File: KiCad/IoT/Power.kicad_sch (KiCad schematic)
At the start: 4 parts, among them J10 5V, J11 3V3, J8 24V, J9 12V

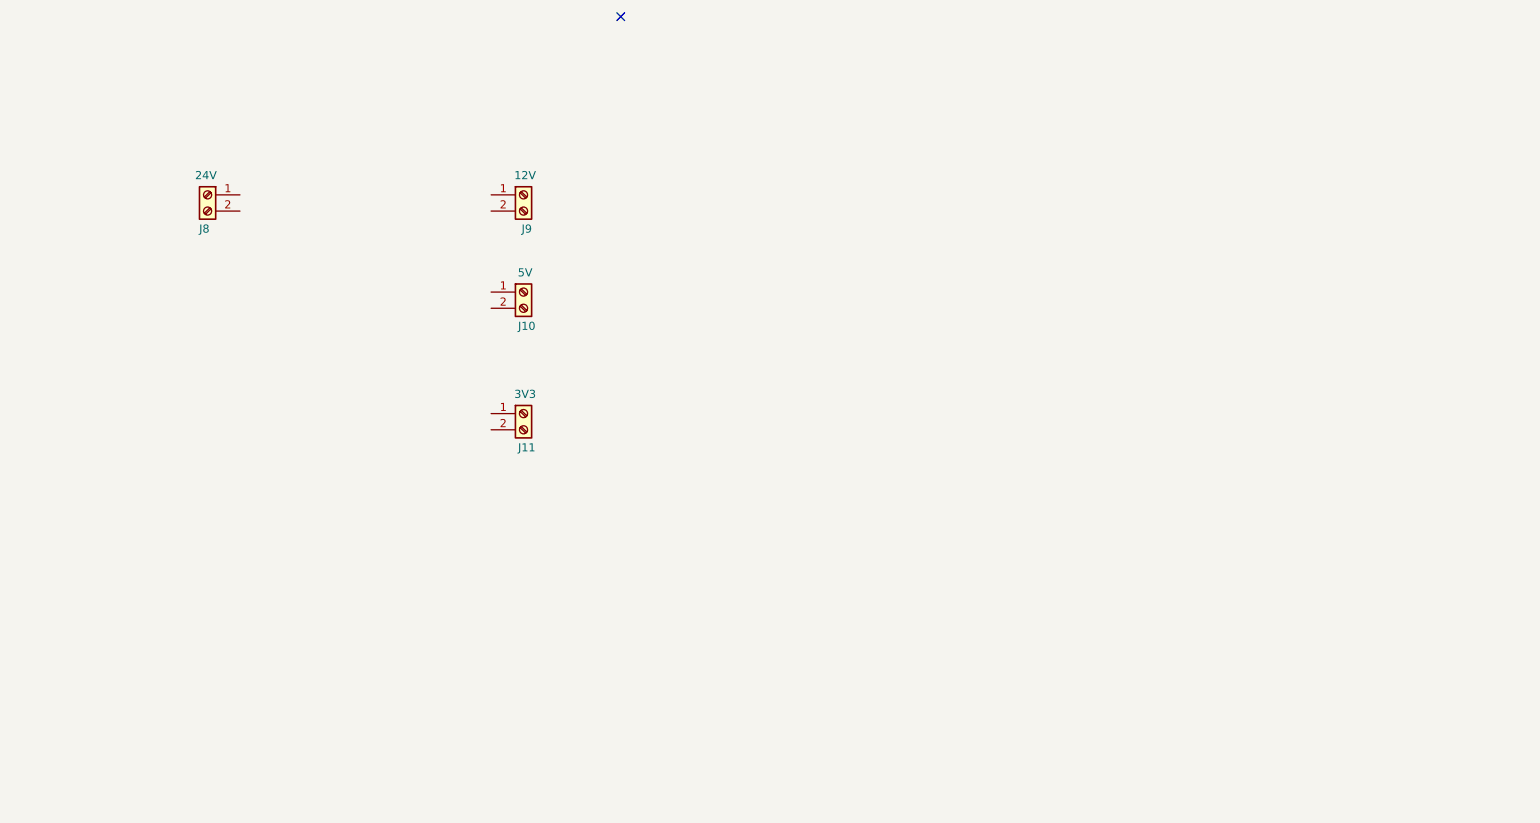
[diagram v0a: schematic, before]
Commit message: updated power schematic
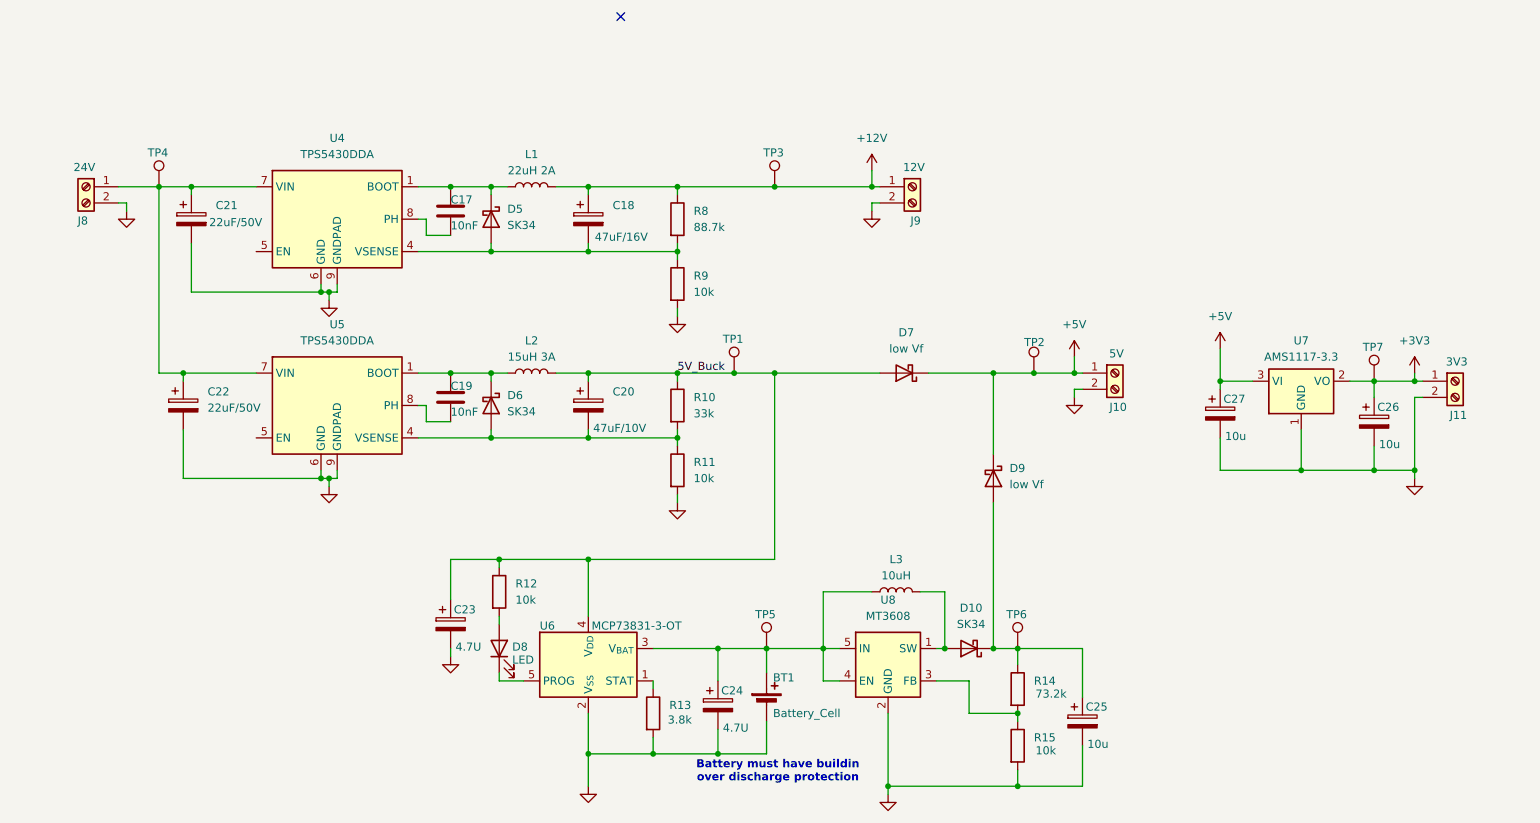
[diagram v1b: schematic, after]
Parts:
- added BT1: Battery_Cell, Battery:BatteryHolder_MPD_BH-18650-PC, symbol Device:Battery_Cell
- added C17, C19: 10nF, symbol Device:C
- added C18: 47uF/16V, Package_SO:SOIC-8_3.9x4.9mm_P1.27mm, symbol Device:C_Polarized
- added C20: 47uF/10V, Package_SO:SOIC-8_3.9x4.9mm_P1.27mm, symbol Device:C_Polarized
- added C21, C22: 22uF/50V, Package_SO:SOIC-8_3.9x4.9mm_P1.27mm, symbol Device:C_Polarized
- added C23, C24: 4.7U, Package_SO:SOIC-8_3.9x4.9mm_P1.27mm, symbol Device:C_Polarized
- added C25, C26, C27: 10u, Package_SO:SOIC-8_3.9x4.9mm_P1.27mm, symbol Device:C_Polarized
- added D10, D5, D6: SK34, Package_SON:WSON-8-1EP_6x5mm_P1.27mm_EP3.4x4mm, symbol Device:D_Schottky
- added D7, D9: low Vf, Package_SON:WSON-8-1EP_6x5mm_P1.27mm_EP3.4x4mm, symbol Device:D_Schottky
- added D8: LED, LED_SMD:LED_Cree-XHP50_3V_HighDensity, symbol Device:LED
- added L1: 22uH 2A, symbol Device:L
- added L2: 15uH 3A, symbol Device:L
- added L3: 10uH, Package_TO_SOT_SMD:SOT-23-6, symbol Device:L
- added R10: 33k, symbol Device:R
- added R11, R12, R15, R9: 10k, symbol Device:R
- added R13: 3.8k, symbol Device:R
- added R14: 73.2k, symbol Device:R
- added R8: 88.7k, symbol Device:R
- added TP1, TP2, TP3, TP4, TP5, TP6, TP7: TestPoint, Connector_Pin:Pin_D0.7mm_L6.5mm_W1.8mm_FlatFork, symbol Connector:TestPoint
- added U4, U5: TPS5430DDA, Package_SO:TI_SO-PowerPAD-8_ThermalVias, symbol Regulator_Switching:TPS5430DDA
- added U6: MCP73831-3-OT, Package_TO_SOT_SMD:SOT-23-5, symbol Battery_Management:MCP73831-3-OT
- added U7: AMS1117-3.3, Package_TO_SOT_SMD:SOT-223-3_TabPin2, symbol Regulator_Linear:AMS1117-3.3
- added U8: MT3608, Package_TO_SOT_SMD:SOT-23-6, symbol Regulator_Switching:MT3608
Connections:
- net +12V: now reaches J9.1 (Pin_1)
- net +12V: now also C18.1, L1.2, R8.1, TP3.1
- net GND: now reaches J9.2 (Pin_2)
- net GND: now also J10.2 (Pin_2), J11.2 (Pin_2), J8.2 (Pin_2), BT1.2 (-), C21.2, C22.2, C23.2, C24.2, C25.2, C26.2, C27.2, R11.2, R13.2, R15.2, R9.2, U4.6 (GND), U4.9 (GNDPAD), U5.6 (GND), U5.9 (GNDPAD), U6.2 (V_{SS}), U7.1 (GND), U8.2 (GND)
- net +5V: now reaches J10.1 (Pin_1)
- net +5V: now also C27.1, D7.1 (K), D9.1 (K), TP2.1, U7.3 (VI)
- net +3V3: now reaches J11.1 (Pin_1)
- net +3V3: now also C26.1, TP7.1, U7.2 (VO)
- net at J8.1 (Pin_1): now also C21.1, C22.1, TP4.1, U4.7 (VIN), U5.7 (VIN)
- new net: C18.2, D5.2 (A), R8.2, R9.1, U4.4 (VSENSE)
- new net: C25.1, D10.1 (K), D9.2 (A), R14.1, TP6.1
- new net: C19.1, D6.1 (K), L2.1, U5.1 (BOOT)
- new net: C20.2, D6.2 (A), R10.2, R11.1, U5.4 (VSENSE)
- new net: R14.2, R15.1, U8.3 (FB)
- new net: D10.2 (A), L3.2, U8.1 (SW)
- new net: BT1.1 (+), C24.1, L3.1, TP5.1, U6.3 (V_{BAT}), U8.4 (EN), U8.5 (IN)
- new net: C17.1, D5.1 (K), L1.1, U4.1 (BOOT)
- new net: D8.2 (A), R12.2
- new net: C19.2, U5.8 (PH)
- new net: R13.1, U6.1 (STAT)
- new net: D8.1 (K), U6.5 (PROG)
- new net: C17.2, U4.8 (PH)
- new net 5V_Buck: C20.1, C23.1, D7.2 (A), L2.2, R10.1, R12.1, TP1.1, U6.4 (V_{DD})
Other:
- note added: "Battery must have buildin over discharge protection"
- moved on the sheet: J10, J11, J8, J9

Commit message: added buttons, connected leds, changed uart ic and added crystals
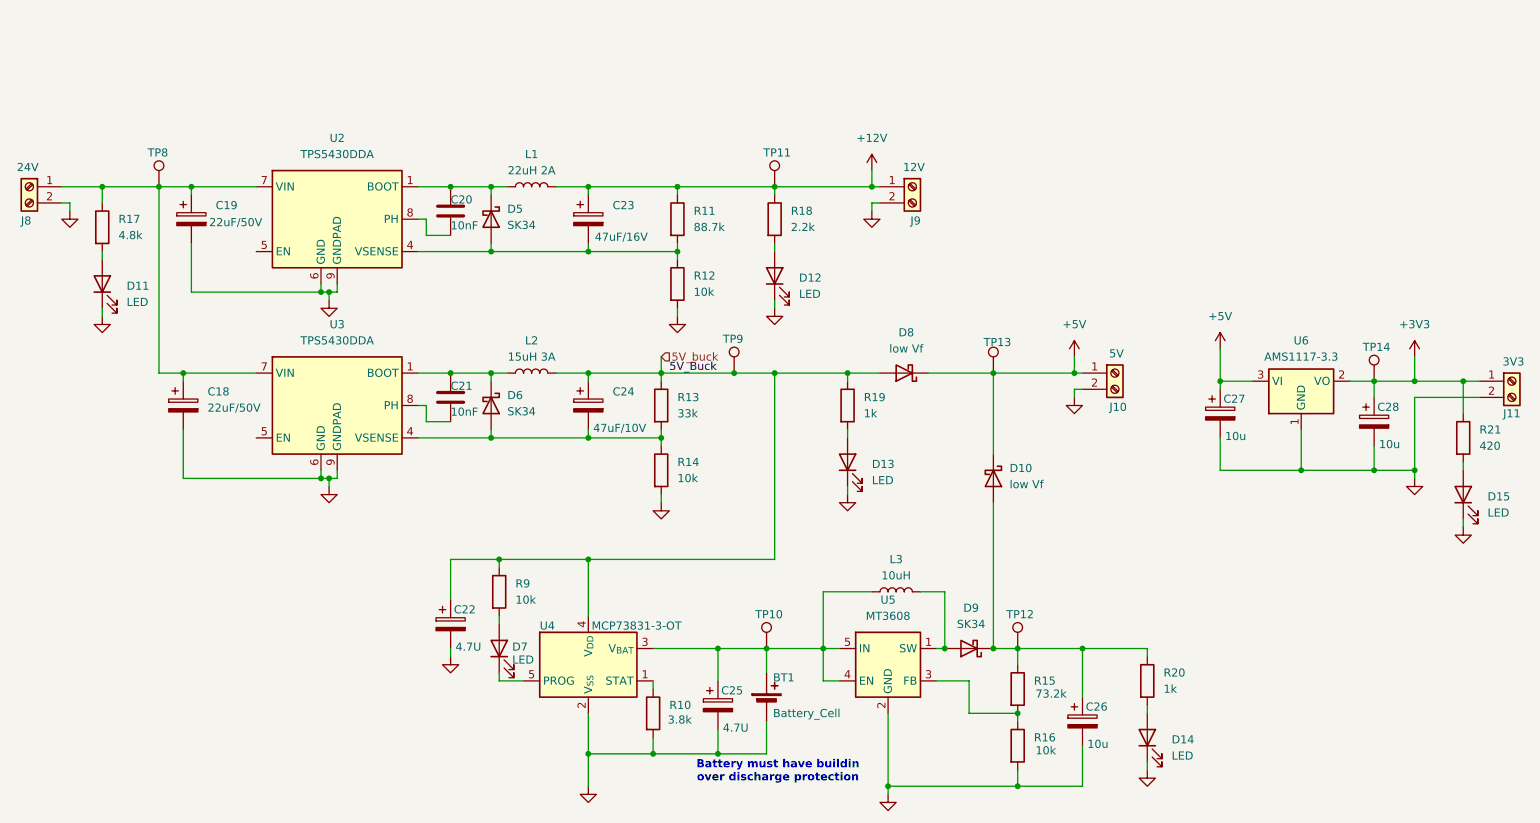
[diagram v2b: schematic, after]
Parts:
- added D11, D12, D13, D14, D15: LED, symbol Device:LED
- added R17: 4.8k, symbol Device:R
- added R18: 2.2k, symbol Device:R
- added R19, R20: 1k, symbol Device:R
- added R21: 420, symbol Device:R
- C19: renamed from C21; footprint Package_SO:SOIC-8_3.9x4.9mm_P1.27mm -> (none)
- C20: renamed from C17; footprint (none) -> Capacitor_SMD:C_0603_1608Metric
- C21: renamed from C19; footprint (none) -> Capacitor_SMD:C_0603_1608Metric
- C22: renamed from C23; footprint Package_SO:SOIC-8_3.9x4.9mm_P1.27mm -> (none)
- C23: renamed from C18; footprint Package_SO:SOIC-8_3.9x4.9mm_P1.27mm -> (none)
- C24: renamed from C20; footprint Package_SO:SOIC-8_3.9x4.9mm_P1.27mm -> (none)
- C25: renamed from C24; footprint Package_SO:SOIC-8_3.9x4.9mm_P1.27mm -> (none)
- C26: renamed from C25; footprint Package_SO:SOIC-8_3.9x4.9mm_P1.27mm -> (none)
- C27: footprint Package_SO:SOIC-8_3.9x4.9mm_P1.27mm -> (none)
- C28: renamed from C26; footprint Package_SO:SOIC-8_3.9x4.9mm_P1.27mm -> (none)
- D10: renamed from D9; footprint Package_SON:WSON-8-1EP_6x5mm_P1.27mm_EP3.4x4mm -> (none)
- D5, D6: footprint Package_SON:WSON-8-1EP_6x5mm_P1.27mm_EP3.4x4mm -> (none)
- D7: renamed from D8; footprint LED_SMD:LED_Cree-XHP50_3V_HighDensity -> (none)
- D8: renamed from D7; footprint Package_SON:WSON-8-1EP_6x5mm_P1.27mm_EP3.4x4mm -> (none)
- D9: renamed from D10; footprint Package_SON:WSON-8-1EP_6x5mm_P1.27mm_EP3.4x4mm -> (none)
- renumbered C22 to C18, R13 to R10, R8 to R11, R9 to R12, R10 to R13, R11 to R14, R14 to R15, R15 to R16, R12 to R9, TP5 to TP10, TP3 to TP11, TP6 to TP12, TP2 to TP13, TP7 to TP14, TP4 to TP8, TP1 to TP9, U4 to U2, U5 to U3, U6 to U4, U8 to U5, U7 to U6
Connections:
- net +12V: now also R18.1
- net +3V3: now also R21.1
- net GND: now also D11.1 (K), D12.1 (K), D13.1 (K), D14.1 (K), D15.1 (K)
- net at C26.1, D10.2 (A), D9.1 (K)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: now also R20.1
- net at C18.1, C19.1, J8.1 (Pin_1)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: now also R17.1
- net 5V_Buck renamed 5V_buck
- net 5V_buck: now also R19.1
- new net: D11.2 (A), R17.2
- new net: D12.2 (A), R18.2
- new net: D14.2 (A), R20.2
- new net: D15.2 (A), R21.2
- new net: D13.2 (A), R19.2
- no-connect marks 1 -> 0
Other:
- moved on the sheet: J11, J8, R13, R14, TP13

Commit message: minor fixes and cleanup
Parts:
- renumbered C18 to C23, C19 to C24, C20 to C25, C21 to C26, C22 to C27, C23 to C28, C24 to C29, C25 to C30, C26 to C31, C27 to C32, C28 to C33, D12 to D10, D13 to D11, D8 to D12, D9 to D13, D10 to D14, D14 to D15, D15 to D16, D11 to D6, D5 to D7, D6 to D8, D7 to D9, J9 to J10, J10 to J11, J11 to J12, J8 to J9, R17 to R16, R9 to R17, R10 to R18, R13 to R19, R14 to R20, R11 to R21, R12 to R22, R18 to R23, R19 to R24, R15 to R25, R16 to R26, R20 to R27, R21 to R28, TP13 to TP12, TP12 to TP13

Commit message: circuit bugfixes
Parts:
- C34: renamed from C33; value 10u -> 22u
- renumbered C23 to C24, C24 to C25, C25 to C26, C26 to C27, C27 to C28, C28 to C29, C29 to C30, C30 to C31, C31 to C32, C32 to C33, J9 to J17, J10 to J18, J11 to J19, J12 to J20
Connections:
- net at U4.1 (STAT): now also D9.1 (K); no longer R18.1
- net at U4.5 (PROG): now also R18.1; no longer D9.1 (K)
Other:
- moved on the sheet: C28, D9, R17, R18
